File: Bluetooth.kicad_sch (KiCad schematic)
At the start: 5 parts, among them J4 SWD, U9 BLUENRG-M2SA

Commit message: layout rearranging
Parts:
- removed J4: SWD, Connector_PinHeader_2.54mm:PinHeader_1x04_P2.54mm_Vertical, symbol Connector_Generic:Conn_01x04
- added C39: 10u, Capacitor_SMD:C_0805_2012Metric, symbol Device:C
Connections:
- net +3.3V: now also C39.1
- net GND: now also C39.2
- net SWCLK: no longer names the net of U9.12 (DIO9)
- net SWDIO: no longer names the net of U9.13 (DIO10)
- no-connect marks 16 -> 18
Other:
- note added: "RC circuit for reset timing, external reset can be attached"
- note added: "choose pcb antenna!!"
- note removed: "Flashing pins"
- note removed: "RC circuit for reset timing"
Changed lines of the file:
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@@
   (junction (at 114.3 119.38) (diameter 0) (color 0 0 0 0)
+  )
+  (junction (at 96.52 98.425) (diameter 0) (color 0 0 0 0)
   )
   (no_connect (at 101.6 81.915))
@@
   (no_connect (at 101.6 79.375))
   (no_connect (at 119.38 59.055))
+  (no_connect (at 127 117.475))
   (no_connect (at 101.6 84.455))
+  (no_connect (at 124.46 117.475))
   (no_connect (at 137.16 89.535))
   (no_connect (at 109.22 117.475))
   (no_connect (at 137.16 86.995))
   (no_connect (at 116.84 117.475))
-  (wire (pts (xy 186.69 96.52) (xy 189.23 96.52))
-    (stroke (width 0) (type default))
-  )
   (wire (pts (xy 137.16 79.375) (xy 142.24 79.375))
     (stroke (width 0) (type default))
   )
+  (wire (pts (xy 86.36 86.995) (xy 96.52 86.995))
+    (stroke (width 0) (type default))
+  )
   (wire (pts (xy 119.38 123.825) (xy 119.38 117.475))
     (stroke (width 0) (type default))
   )
-  (wire (pts (xy 96.52 119.38) (xy 96.52 96.52))
-    (stroke (width 0) (type default))
-  )
-  (wire (pts (xy 177.8 93.98) (xy 189.23 93.98))
-    (stroke (width 0) (type default))
-  )
-  (wire (pts (xy 186.69 88.9) (xy 189.23 88.9))
+  (wire (pts (xy 96.52 119.38) (xy 96.52 98.425))
+    (stroke (width 0) (type default))
+  )
+  (wire (pts (xy 96.52 98.425) (xy 96.52 96.52))
     (stroke (width 0) (type default))
   )
@@
     (stroke (width 0) (type default))
   )
-  (wire (pts (xy 186.69 99.695) (xy 186.69 96.52))
-    (stroke (width 0) (type default))
-  )
   (wire (pts (xy 142.24 76.835) (xy 142.24 79.375))
     (stroke (width 0) (type default))
@@
     (stroke (width 0) (type default))
   )
+  (wire (pts (xy 86.36 96.52) (xy 86.36 98.425))
+    (stroke (width 0) (type default))
+  )
   (wire (pts (xy 96.52 86.995) (xy 101.6 86.995))
     (stroke (width 0) (type default))
@@
     (stroke (width 0) (type default))
   )
-  (wire (pts (xy 189.23 91.44) (xy 177.8 91.44))
+  (wire (pts (xy 86.36 88.9) (xy 86.36 86.995))
     (stroke (width 0) (type default))
   )
@@
     (stroke (width 0) (type default))
   )
-  (wire (pts (xy 186.69 85.725) (xy 186.69 88.9))
-    (stroke (width 0) (type default))
-  )
   (wire (pts (xy 142.24 67.31) (xy 142.24 69.215))
     (stroke (width 0) (type default))
   )
-  (text "RC circuit for reset timing" (at 133.35 99.695 0)
+  (wire (pts (xy 86.36 98.425) (xy 96.52 98.425))
+    (stroke (width 0) (type default))
+  )
+  (text "RC circuit for reset timing,\nexternal reset can be attached"
+    (at 133.35 100.965 0)
     (effects (font (size 1.27 1.27)) (justify left bottom))
   )
@@
     (effects (font (size 2.54 2.54) (thickness 0.508) bold) (justify left bottom))
   )
+  (text "choose pcb antenna!!" (at 51.435 93.98 0)
+    (effects (font (size 1.27 1.27)) (justify left bottom))
+  )
   (text "***SOC datasheet" (at 94.615 55.88 0)
     (effects (font (size 1.27 1.27)) (justify left bottom) (href "https://www.st.com/resource/en/datasheet/bluenrg-2.pdf"))
-  )
-  (text "Flashing pins" (at 180.975 110.49 0)
-    (effects (font (size 1.27 1.27)) (justify left bottom))
-  )
-  (label "SWDIO" (at 177.8 93.98 180) (fields_autoplaced)
-    (effects (font (size 1.27 1.27)) (justify right bottom))
-  )
-  (label "SWDIO" (at 127 117.475 270) (fields_autoplaced)
-    (effects (font (size 1.27 1.27)) (justify right bottom))
-  )
-  (label "SWCLK" (at 124.46 117.475 270) (fields_autoplaced)
-    (effects (font (size 1.27 1.27)) (justify right bottom))
-  )
-  (label "SWCLK" (at 177.8 91.44 180) (fields_autoplaced)
-    (effects (font (size 1.27 1.27)) (justify right bottom))
   )
   (hierarchical_label "UART_TX" (shape output) (at 119.38 123.825 270) (fields_autoplaced)
@@
     )
   )
-  (symbol (lib_id "power:GND") (at 186.69 99.695 0) (unit 1)
-    (in_bom yes) (on_board yes) (dnp no)
-    (property "Reference" "#PWR017" (at 186.69 106.045 0)
-      (effects (font (size 1.27 1.27)) hide)
-    )
-    (property "Value" "GND" (at 186.817 104.0892 0)
-      (effects (font (size 1.27 1.27)))
-    )
-    (property "Footprint" "" (at 186.69 99.695 0)
-      (effects (font (size 1.27 1.27)) hide)
-    )
-    (property "Datasheet" "" (at 186.69 99.695 0)
-      (effects (font (size 1.27 1.27)) hide)
-    )
-    (pin "1")
-    (instances
-      (project "Telemetry-Primary"
-        (path "/7f2a449b-14af-42b3-8d38-5f0f8a5ee7ce"
-          (reference "#PWR017") (unit 1)
-        )
-        (path "/7f2a449b-14af-42b3-8d38-5f0f8a5ee7ce/57884461-52ec-4fdf-8849-cb39fe7f004b"
-          (reference "#PWR030") (unit 1)
-        )
-      )
-    )
-  )
   (symbol (lib_id "power:+3.3V") (at 96.52 67.31 0) (unit 1)
     (in_bom yes) (on_board yes) (dnp no)
@@
     )
   )
-  (symbol (lib_id "power:+3.3V") (at 186.69 85.725 0) (unit 1)
-    (in_bom yes) (on_board yes) (dnp no)
-    (property "Reference" "#PWR016" (at 186.69 89.535 0)
-      (effects (font (size 1.27 1.27)) hide)
-    )
-    (property "Value" "+3.3V" (at 187.071 81.3308 0)
-      (effects (font (size 1.27 1.27)))
-    )
-    (property "Footprint" "" (at 186.69 85.725 0)
-      (effects (font (size 1.27 1.27)) hide)
-    )
-    (property "Datasheet" "" (at 186.69 85.725 0)
-      (effects (font (size 1.27 1.27)) hide)
-    )
-    (pin "1")
-    (instances
-      (project "Telemetry-Primary"
-        (path "/7f2a449b-14af-42b3-8d38-5f0f8a5ee7ce"
-          (reference "#PWR016") (unit 1)
-        )
-        (path "/7f2a449b-14af-42b3-8d38-5f0f8a5ee7ce/57884461-52ec-4fdf-8849-cb39fe7f004b"
-          (reference "#PWR027") (unit 1)
-        )
-      )
-    )
-  )
   (symbol (lib_id "power:GND") (at 142.24 91.44 0) (unit 1)
     (in_bom yes) (on_board yes) (dnp no)
@@
         (path "/c248b171-df31-4e8a-afb6-607fa2df334b/00000000-0000-0000-0000-00005f24b488"
           (reference "#PWR0102") (unit 1)
-        )
-      )
-    )
-  )
-  (symbol (lib_id "Connector_Generic:Conn_01x04") (at 194.31 91.44 0) (unit 1)
-    (in_bom yes) (on_board yes) (dnp no)
-    (property "Reference" "J4" (at 196.342 91.6432 0)
-      (effects (font (size 1.27 1.27)) (justify left))
-    )
-    (property "Value" "SWD" (at 196.342 93.9546 0)
-      (effects (font (size 1.27 1.27)) (justify left))
-    )
-    (property "Footprint" "Connector_PinHeader_2.54mm:PinHeader_1x04_P2.54mm_Vertical" (at 194.31 91.44 0)
-      (effects (font (size 1.27 1.27)) hide)
-    )
-    (property "Datasheet" "https://cdn.amphenol-cs.com/media/wysiwyg/files/documentation/datasheet/boardwiretoboard/bwb_econostik_254headers.pdf" (at 194.31 91.44 0)
-      (effects (font (size 1.27 1.27)) hide)
-    )
-    (property "P/N" "10129378-910001BLF" (at 194.31 91.44 0)
-      (effects (font (size 1.27 1.27)) hide)
-    )
-    (pin "1")
-    (pin "2")
-    (pin "3")
-    (pin "4")
-    (instances
-      (project "Telemetry-Primary"
-        (path "/7f2a449b-14af-42b3-8d38-5f0f8a5ee7ce"
-          (reference "J4") (unit 1)
-        )
-        (path "/7f2a449b-14af-42b3-8d38-5f0f8a5ee7ce/57884461-52ec-4fdf-8849-cb39fe7f004b"
-          (reference "J13") (unit 1)
         )
       )
@@
         )
       )
+    )
+  )
+  (symbol (lib_id "Device:C") (at 86.36 92.71 0) (unit 1)
+    (in_bom yes) (on_board yes) (dnp no)
+    (property "Reference" "C39" (at 89.281 91.5416 0)
+      (effects (font (size 1.27 1.27)) (justify left))
+    )
+    (property "Value" "10u" (at 89.281 93.853 0)
+      (effects (font (size 1.27 1.27)) (justify left))
+    )
+    (property "Footprint" "Capacitor_SMD:C_0805_2012Metric" (at 87.3252 96.52 0)
+      (effects (font (size 1.27 1.27)) hide)
+    )
+    (property "Datasheet" "https://www.mouser.com/datasheet/2/212/KEM_C1002_X7R_SMD-1102033.pdf" (at 86.36 92.71 0)
+      (effects (font (size 1.27 1.27)) hide)
+    )
+    (property "P/N" "C0805C104K5RAC7411" (at 86.36 92.71 0)
+      (effects (font (size 1.27 1.27)) hide)
+    )
+    (pin "1")
+    (pin "2")
+    (instances
+      (project "Telemetry-Primary"
+        (path "/7f2a449b-14af-42b3-8d38-5f0f8a5ee7ce/00000000-0000-0000-0000-00005f6dd18a"
+          (reference "C39") (unit 1)
+        )
+        (path "/7f2a449b-14af-42b3-8d38-5f0f8a5ee7ce/57884461-52ec-4fdf-8849-cb39fe7f004b"
+          (reference "C63") (unit 1)
+        )
+      )

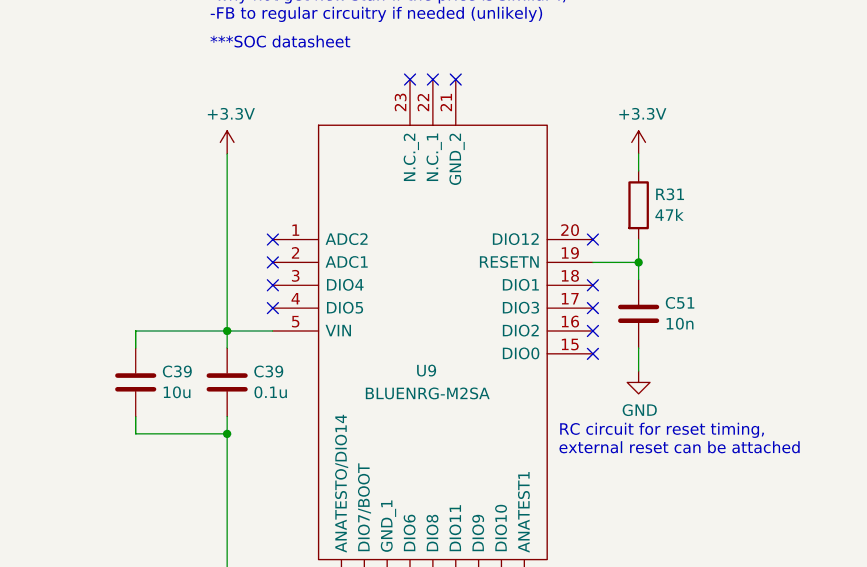
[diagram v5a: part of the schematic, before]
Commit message: inputs routing + fixed models + clock keepouts
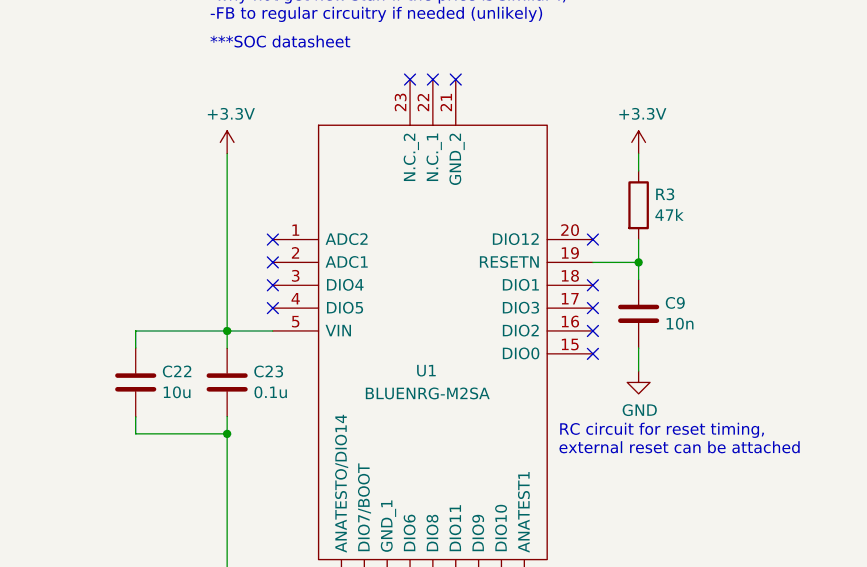
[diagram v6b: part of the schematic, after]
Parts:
- U1: renamed from U9; footprint BLUENRGM2SA -> UTSVT_ICs:BLUENRGM2SA
- renumbered C39 to C22, C39 to C23, C51 to C9, R31 to R3
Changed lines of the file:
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@@
   (symbol (lib_id "Device:C") (at 96.52 92.71 0) (unit 1)
     (in_bom yes) (on_board yes) (dnp no)
-    (property "Reference" "C39" (at 99.441 91.5416 0)
+    (property "Reference" "C23" (at 99.441 91.5416 0)
       (effects (font (size 1.27 1.27)) (justify left))
     )
@@
       (project "Telemetry-Primary"
         (path "/7f2a449b-14af-42b3-8d38-5f0f8a5ee7ce/57884461-52ec-4fdf-8849-cb39fe7f004b"
-          (reference "C62") (unit 1)
+          (reference "C23") (unit 1)
         )
       )
@@
   (symbol (lib_id "Device:R") (at 142.24 73.025 0) (unit 1)
     (in_bom yes) (on_board yes) (dnp no)
-    (property "Reference" "R31" (at 144.018 71.8566 0)
+    (property "Reference" "R3" (at 144.018 71.8566 0)
       (effects (font (size 1.27 1.27)) (justify left))
     )
@@
       (project "Telemetry-Primary"
         (path "/7f2a449b-14af-42b3-8d38-5f0f8a5ee7ce/57884461-52ec-4fdf-8849-cb39fe7f004b"
-          (reference "R31") (unit 1)
+          (reference "R3") (unit 1)
         )
       )
@@
   (symbol (lib_id "BLUENRG-M2SA:BLUENRG-M2SA") (at 101.6 76.835 0) (unit 1)
     (in_bom yes) (on_board yes) (dnp no)
-    (property "Reference" "U9" (at 117.475 91.44 0)
+    (property "Reference" "U1" (at 117.475 91.44 0)
       (effects (font (size 1.27 1.27)) (justify left))
     )
@@
       (effects (font (size 1.27 1.27)) (justify left))
     )
-    (property "Footprint" "BLUENRGM2SA" (at 133.35 64.135 0)
+    (property "Footprint" "UTSVT_ICs:BLUENRGM2SA" (at 133.35 64.135 0)
       (effects (font (size 1.27 1.27)) (justify left) hide)
     )
@@
       (project "Telemetry-Primary"
         (path "/7f2a449b-14af-42b3-8d38-5f0f8a5ee7ce/57884461-52ec-4fdf-8849-cb39fe7f004b"
-          (reference "U9") (unit 1)
+          (reference "U1") (unit 1)
         )
       )
@@
   (symbol (lib_id "Device:C") (at 86.36 92.71 0) (unit 1)
     (in_bom yes) (on_board yes) (dnp no)
-    (property "Reference" "C39" (at 89.281 91.5416 0)
+    (property "Reference" "C22" (at 89.281 91.5416 0)
       (effects (font (size 1.27 1.27)) (justify left))
     )
@@
       (project "Telemetry-Primary"
         (path "/7f2a449b-14af-42b3-8d38-5f0f8a5ee7ce/57884461-52ec-4fdf-8849-cb39fe7f004b"
-          (reference "C63") (unit 1)
+          (reference "C22") (unit 1)
         )
       )
@@
   (symbol (lib_id "Device:C") (at 142.24 85.09 0) (unit 1)
     (in_bom yes) (on_board yes) (dnp no)
-    (property "Reference" "C51" (at 145.161 83.9216 0)
+    (property "Reference" "C9" (at 145.161 83.9216 0)
       (effects (font (size 1.27 1.27)) (justify left))
     )
@@
       (project "Telemetry-Primary"
         (path "/7f2a449b-14af-42b3-8d38-5f0f8a5ee7ce/57884461-52ec-4fdf-8849-cb39fe7f004b"
-          (reference "C51") (unit 1)
-        )
-      )
+          (reference "C9") (unit 1)
+        )
+      )
